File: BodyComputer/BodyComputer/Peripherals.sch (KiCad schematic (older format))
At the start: 17 parts

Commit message: Update due to moving to another computer. Updated Schematic, Print-outs, PCB in development
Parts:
- added J13, J9: Conn_02x05_Odd_Even, Connector_IDC:IDC-Header_2x05_P2.54mm_Vertical, symbol Connector_Generic:Conn_02x05_Odd_Even
- added J35: Conn_01x02, Connector_PinSocket_2.54mm:PinSocket_1x02_P2.54mm_Vertical, symbol Connector_Generic:Conn_01x02
- D11: renamed from D?; footprint (none) -> Diode_SMD:D_0603_1608Metric_Pad1.05x0.95mm_HandSolder
- SW1: renamed from SW?; footprint (none) -> Button_Switch_THT:SW_PUSH_6mm
- gave numbers to parts that had none: 15
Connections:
- net +3V3: now also J14.3 (Pin_3), J14.5 (Pin_5), J14.7 (Pin_7)
- net GND: now also J14.1 (Pin_1), J14.10 (Pin_10), J14.9 (Pin_9), J13.6 (Pin_6), J35.2 (Pin_2), J9.6 (Pin_6)
- net MISO: now also J11.2; no longer J11.3
- net MOSI: now also J11.3; no longer J11.4
- net RESET_BUTTON: now also J9.8 (Pin_8)
- net RX: now also J11.5; no longer J11.1
- net SCK: now also J11.1; no longer J11.5
- net TX: now also J11.4; no longer J11.2
- net at U5.1 (A0(ADC0)): now also J9.9 (Pin_9)
- net at U5.11 (3.3V): now also J9.10 (Pin_10)
- net at U5.18 (TX(GPIO1)): now also J13.2 (Pin_2)
- net at U5.19 (RX(DPIO3)): now also J13.4 (Pin_4)
- net at U5.22 (D6(GPIO12)): now also J13.8 (Pin_8)
- net at U5.23 (D5(GPIO14)): now also J13.10 (Pin_10)
- net at U5.25 (3.3V): now also J13.9 (Pin_9)
- net at U5.26 (D4(GPIO2)): now also J13.7 (Pin_7)
- net at U5.27 (D3(GPIO0)): now also J13.5 (Pin_5)
- net at U5.28 (D2(GPIO4)): now also J13.3 (Pin_3)
- net at U5.29 (D1(GPIO5)): now also J13.1 (Pin_1)
- net at U5.4 (SD3(GPIO10)): now also J9.7 (Pin_7)
- net at U5.5 (SD2(GPIO9)): now also J9.5 (Pin_5)
- net at U5.6 (SD1(MOSI)): now also J9.3 (Pin_3)
- net at U5.7 (CMD(CS)): now also J9.1 (Pin_1)
- net at U5.8 (SDO(MISO)): now also J9.2 (Pin_2)
- net at U5.9 (CLK(SCLK)): now also J9.4 (Pin_4)
- new net VIN: J35.1 (Pin_1)
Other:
- note added: "FAN connector"
- note added: "NodeMCU v3 and external connectors (IDC10)"
- moved on the sheet: D11, J14, R27, U5

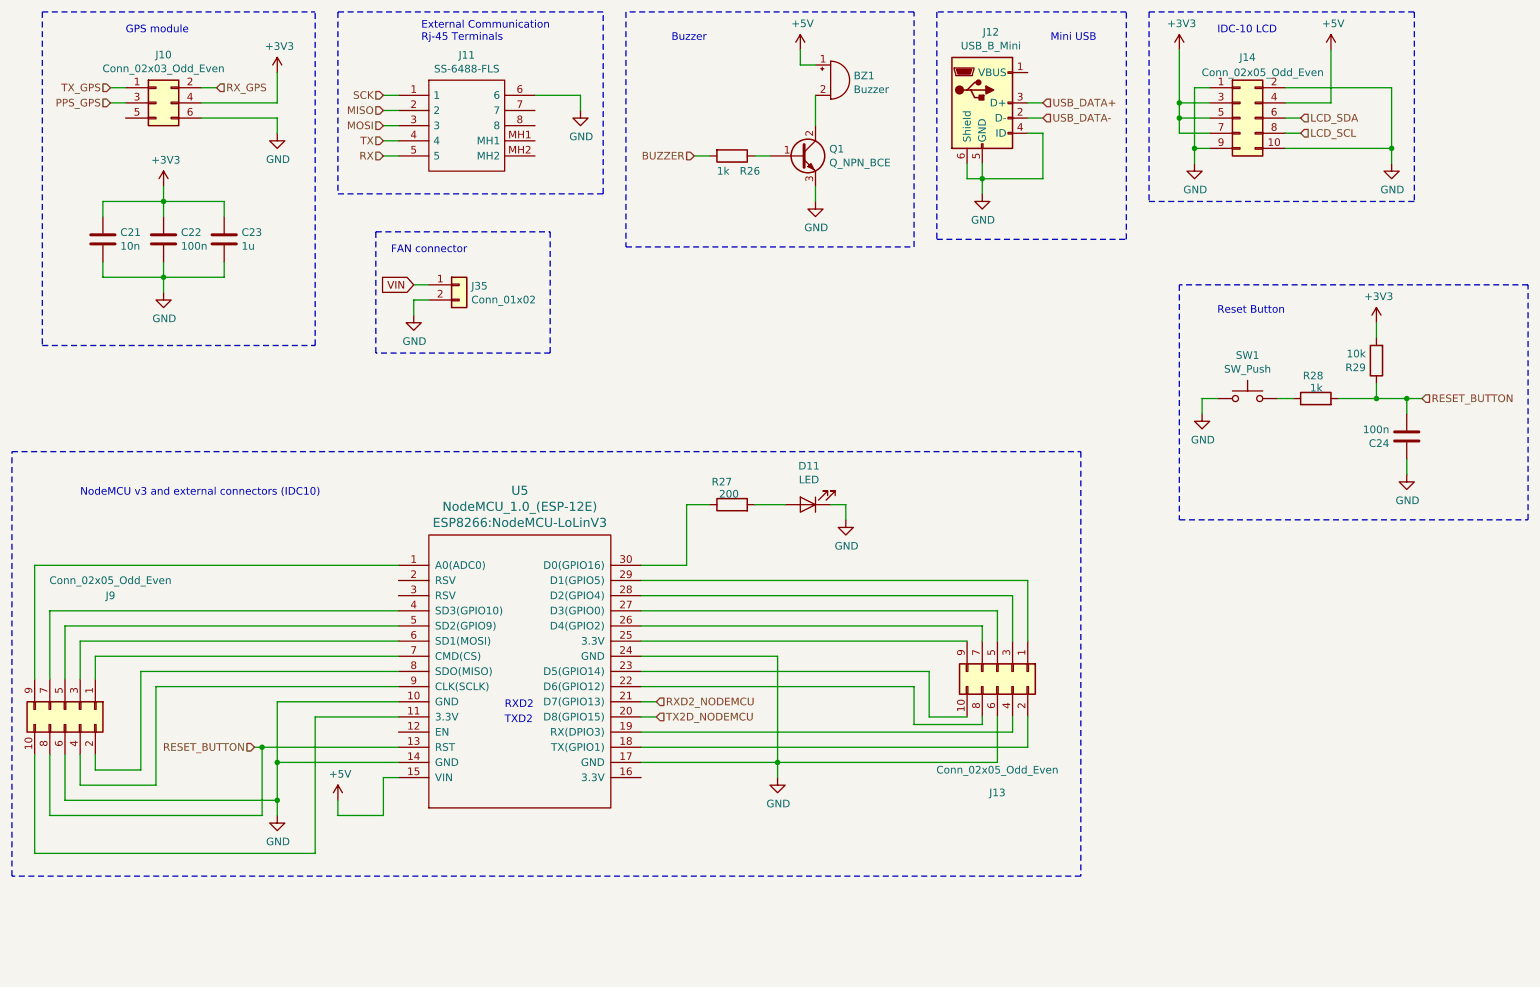
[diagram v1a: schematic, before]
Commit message: Updated schematic (DC/DC), 2-layer PCB
Updated schematic in multiple places, added elements, exchanged 3V3 stabilizer for a DC/DC converter. Nearly finished 2-layer PCB layout.
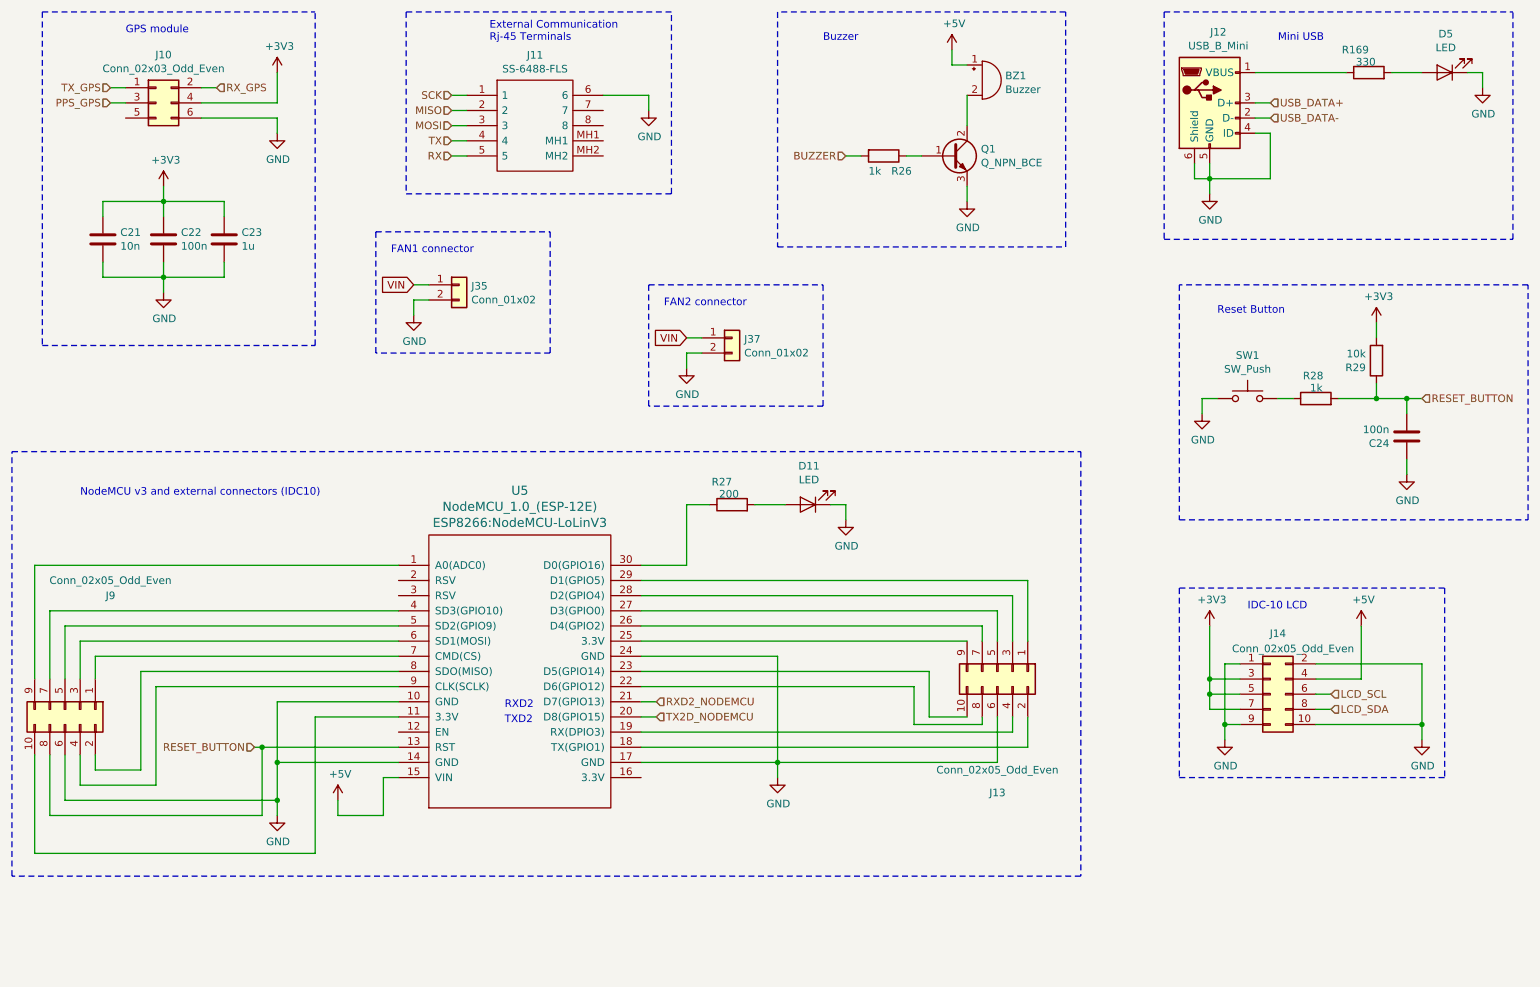
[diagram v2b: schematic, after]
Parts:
- added D5: LED, Diode_SMD:D_0603_1608Metric_Pad1.05x0.95mm_HandSolder, symbol Device:LED
- added J37: Conn_01x02, Connector_PinSocket_2.54mm:PinSocket_1x02_P2.54mm_Vertical, symbol Connector_Generic:Conn_01x02
- added R169: 330, Resistor_SMD:R_0603_1608Metric, symbol Device:R
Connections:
- net GND: now also D5.1 (K), J37.2 (Pin_2)
- net LCD_SCL: now also J14.6 (Pin_6); no longer J14.8 (Pin_8)
- net LCD_SDA: now also J14.8 (Pin_8); no longer J14.6 (Pin_6)
- net VIN: now also J37.1 (Pin_1)
- net at J12.1 (VBUS): now also R169.1
- new net: D5.2 (A), R169.2
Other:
- note added: "FAN1 connector"
- note added: "FAN2 connector"
- note removed: "FAN connector"
- moved on the sheet: BZ1, J11, J12, J14, Q1, R26

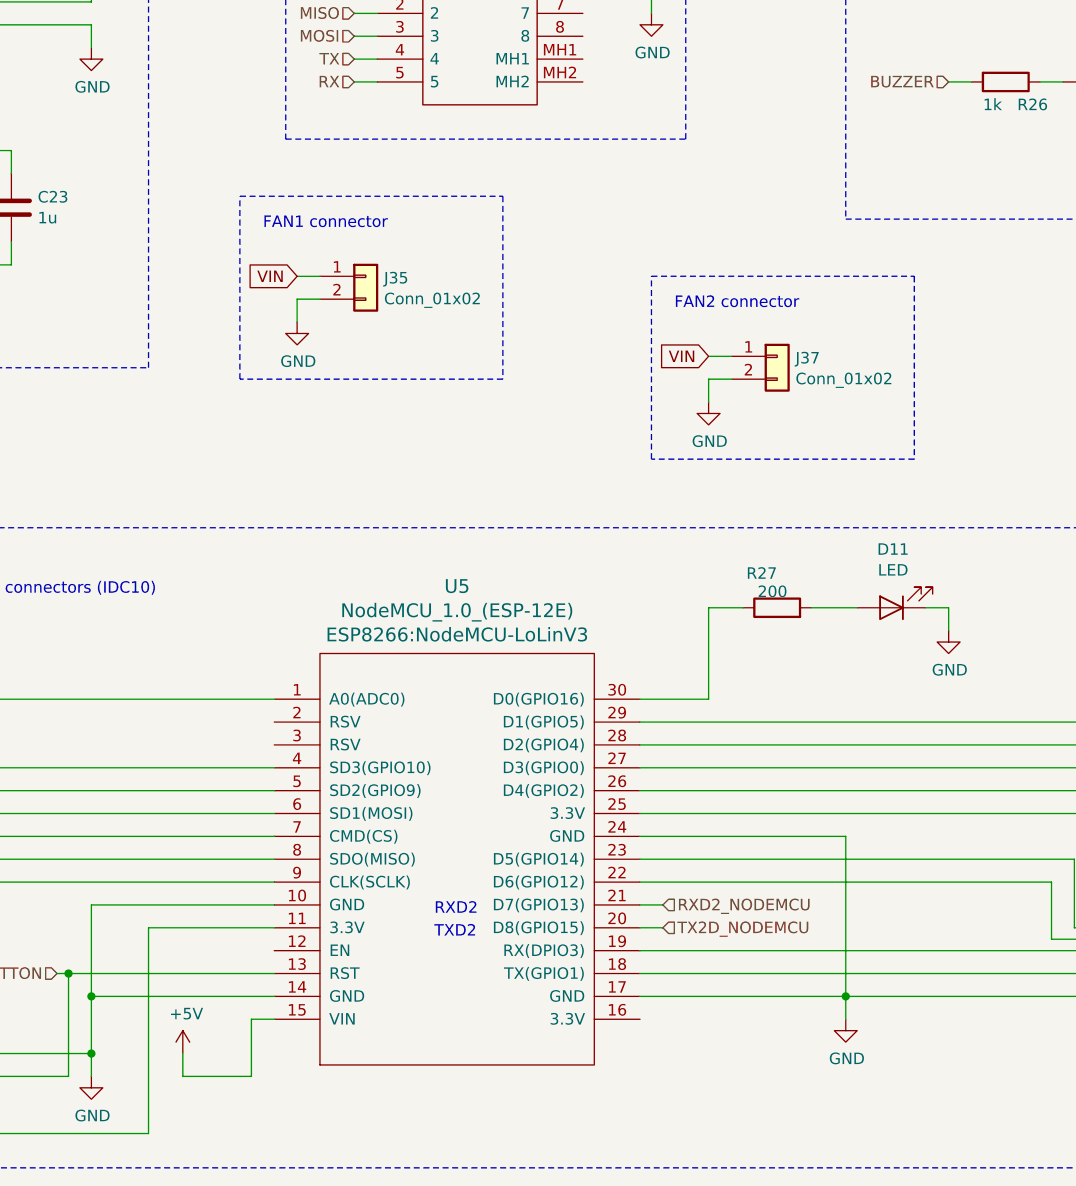
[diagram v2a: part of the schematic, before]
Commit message: Body Computer - 4layer
Added 4-layer board layout, changed schematic a bit, added jumper for NodeMCU powering, control MOSFET for Fans
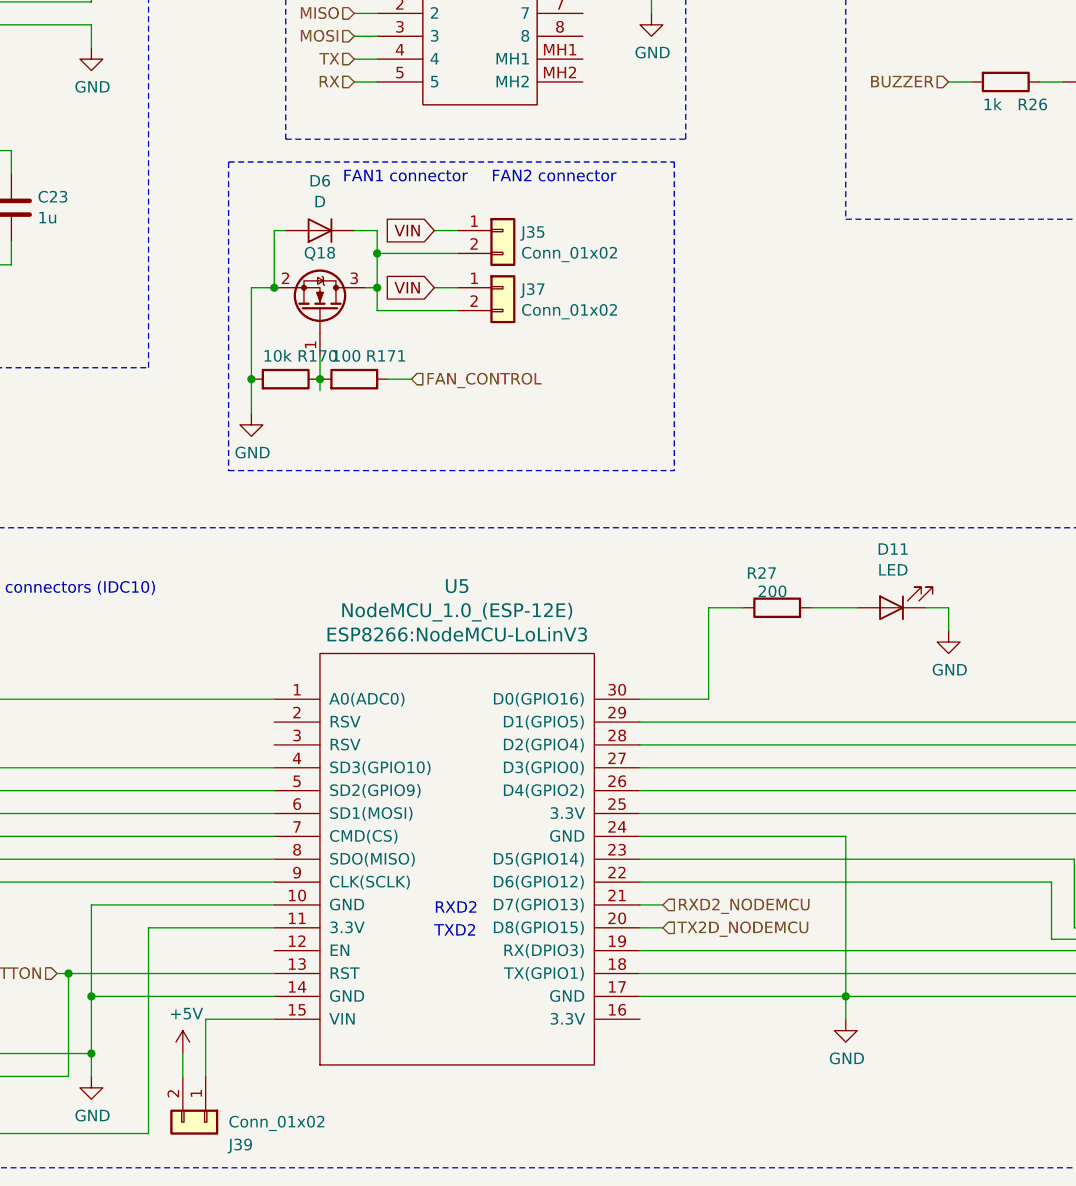
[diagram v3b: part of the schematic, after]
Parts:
- added D6: D, Diode_SMD:D_SMA, symbol Device:D
- added J39: Conn_01x02, Connector_PinSocket_2.54mm:PinSocket_1x02_P2.54mm_Vertical, symbol Connector_Generic:Conn_01x02
- added Q18: IRLML2060, Package_TO_SOT_SMD:SOT-23, symbol Transistor_FET:IRLML2060
- added R170: 10k, Resistor_SMD:R_0603_1608Metric, symbol Device:R
- added R171: 100, Resistor_SMD:R_0603_1608Metric, symbol Device:R
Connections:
- net +5V: now also J39.2 (Pin_2); no longer U5.15 (VIN)
- net GND: now also D6.2 (A), Q18.2 (S), R170.2; no longer J35.2 (Pin_2), J37.2 (Pin_2)
- new net: J39.1 (Pin_1), U5.15 (VIN)
- new net: D6.1 (K), J35.2 (Pin_2), J37.2 (Pin_2), Q18.3 (D)
- new net: Q18.1 (G), R170.1, R171.2
- new net FAN_CONTROL: R171.1
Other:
- moved on the sheet: J35, J37
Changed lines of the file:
@@
 Sheet 4 7
 Title "Body Computer"
-Date "2020-04-01"
+Date "2020-04-12"
 Rev "1.0"
 Comp "Wojciech Grzeliński"
@@
 $EndComp
 Wire Wire Line
-	3350 5750 3250 5750
-Wire Wire Line
-	3250 5750 3250 6000
-Wire Wire Line
-	3250 6000 2950 6000
-Wire Wire Line
 	2950 6000 2950 5900
 Wire Wire Line
@@
 L Connector_Generic:Conn_01x02 J35
 U 1 1 5FE3C840
-P 3750 2500
-F 0 "J35" H 3830 2492 50  0000 L CNN
-F 1 "Conn_01x02" H 3830 2401 50  0000 L CNN
-F 2 "Connector_PinSocket_2.54mm:PinSocket_1x02_P2.54mm_Vertical" H 3750 2500 50  0001 C CNN
-F 3 "~" H 3750 2500 50  0001 C CNN
-	1    3750 2500
-	1    0    0    -1
-$EndComp
-Wire Wire Line
-	3550 2500 3450 2500
-Wire Wire Line
-	3550 2600 3450 2600
-Wire Wire Line
-	3450 2600 3450 2700
-$Comp
-L power:GND #PWR?
-U 1 1 5FE49DD6
-P 3450 2700
-AR Path="/5F25F1A8/5FE49DD6" Ref="#PWR?"  Part="1"
-AR Path="/5E6DC799/5FE49DD6" Ref="#PWR0141"  Part="1"
-F 0 "#PWR0141" H 3450 2450 50  0001 C CNN
-F 1 "GND" H 3455 2527 50  0000 C CNN
-F 2 "" H 3450 2700 50  0001 C CNN
-F 3 "" H 3450 2700 50  0001 C CNN
-	1    3450 2700
-	1    0    0    -1
-$EndComp
-Text GLabel 3450 2500 0    50   Input ~ 0
+P 4350 2300
+F 0 "J35" H 4430 2292 50  0000 L CNN
+F 1 "Conn_01x02" H 4430 2201 50  0000 L CNN
+F 2 "Connector_PinSocket_2.54mm:PinSocket_1x02_P2.54mm_Vertical" H 4350 2300 50  0001 C CNN
+F 3 "~" H 4350 2300 50  0001 C CNN
+	1    4350 2300
+	1    0    0    -1
+$EndComp
+Wire Wire Line
+	4150 2300 4050 2300
+Text GLabel 4050 2300 0    50   Input ~ 0
 VIN
-Text Notes 3300 2300 0    50   ~ 0
+Text Notes 3650 2100 0    50   ~ 0
 FAN1 connector
-Wire Notes Line
-	4350 2150 4350 2950
-Wire Notes Line
-	4350 2950 3200 2950
-Wire Notes Line
-	3200 2950 3200 2150
-Wire Notes Line
-	3200 2150 4350 2150
 $Comp
 L Connector_Generic:Conn_01x02 J37
 U 1 1 5E8F875D
-P 5550 2850
-F 0 "J37" H 5630 2842 50  0000 L CNN
-F 1 "Conn_01x02" H 5630 2751 50  0000 L CNN
-F 2 "Connector_PinSocket_2.54mm:PinSocket_1x02_P2.54mm_Vertical" H 5550 2850 50  0001 C CNN
-F 3 "~" H 5550 2850 50  0001 C CNN
-	1    5550 2850
-	1    0    0    -1
-$EndComp
-Wire Wire Line
-	5350 2850 5250 2850
-Wire Wire Line
-	5350 2950 5250 2950
-Wire Wire Line
-	5250 2950 5250 3050
-$Comp
-L power:GND #PWR?
-U 1 1 5E8F8766
-P 5250 3050
-AR Path="/5F25F1A8/5E8F8766" Ref="#PWR?"  Part="1"
-AR Path="/5E6DC799/5E8F8766" Ref="#PWR0147"  Part="1"
-F 0 "#PWR0147" H 5250 2800 50  0001 C CNN
-F 1 "GND" H 5255 2877 50  0000 C CNN
-F 2 "" H 5250 3050 50  0001 C CNN
-F 3 "" H 5250 3050 50  0001 C CNN
-	1    5250 3050
-	1    0    0    -1
-$EndComp
-Text GLabel 5250 2850 0    50   Input ~ 0
+P 4350 2550
+F 0 "J37" H 4430 2542 50  0000 L CNN
+F 1 "Conn_01x02" H 4430 2451 50  0000 L CNN
+F 2 "Connector_PinSocket_2.54mm:PinSocket_1x02_P2.54mm_Vertical" H 4350 2550 50  0001 C CNN
+F 3 "~" H 4350 2550 50  0001 C CNN
+	1    4350 2550
+	1    0    0    -1
+$EndComp
+Wire Wire Line
+	4150 2550 4050 2550
+Text GLabel 4050 2550 0    50   Input ~ 0
 VIN
-Text Notes 5100 2650 0    50   ~ 0
+Text Notes 4300 2100 0    50   ~ 0
 FAN2 connector
-Wire Notes Line
-	6150 2500 6150 3300
-Wire Notes Line
-	6150 3300 5000 3300
-Wire Notes Line
-	5000 3300 5000 2500
-Wire Notes Line
-	5000 2500 6150 2500
 $Comp
 L Device:R R?
@@
 Wire Notes Line
 	8400 700  10700 700
+$Comp
+L Device:R R?
+U 1 1 5E9991C0
+P 3700 2950
+AR Path="/5E667041/5E9991C0" Ref="R?"  Part="1"
+AR Path="/5E731526/5E9991C0" Ref="R?"  Part="1"
+AR Path="/5E6DC799/5E9991C0" Ref="R171"  Part="1"
+F 0 "R171" V 3800 3000 50  0000 L CNN
+F 1 "100" V 3800 2850 50  0000 L CNN
+F 2 "Resistor_SMD:R_0603_1608Metric" V 3630 2950 50  0001 C CNN
+F 3 "~" H 3700 2950 50  0001 C CNN
+	1    3700 2950
+	0    1    -1   0
+$EndComp
+Wire Wire Line
+	3800 2550 3750 2550
+$Comp
+L Device:D D?
+U 1 1 5E9991CE
+P 3550 2300
+AR Path="/5E731526/5E9991CE" Ref="D?"  Part="1"
+AR Path="/5E6DC799/5E9991CE" Ref="D6"  Part="1"
+F 0 "D6" H 3550 2084 50  0000 C CNN
+F 1 "D" H 3550 2175 50  0000 C CNN
+F 2 "Diode_SMD:D_SMA" H 3550 2300 50  0001 C CNN
+F 3 "~" H 3550 2300 50  0001 C CNN
+	1    3550 2300
+	-1   0    0    1
+$EndComp
+Wire Wire Line
+	3800 2300 3800 2400
+Wire Wire Line
+	3700 2300 3800 2300
+Wire Wire Line
+	3400 2300 3350 2300
+Wire Wire Line
+	3350 2300 3350 2550
+$Comp
+L power:GND #PWR?
+U 1 1 5E9991E5
+P 3250 3100
+AR Path="/5F25F1A8/5E9991E5" Ref="#PWR?"  Part="1"
+AR Path="/5E6DC799/5E9991E5" Ref="#PWR0141"  Part="1"
+AR Path="/5E667041/5E9991E5" Ref="#PWR?"  Part="1"
+AR Path="/5E6671BF/5E9991E5" Ref="#PWR?"  Part="1"
+AR Path="/5E731526/5E9991E5" Ref="#PWR?"  Part="1"
+F 0 "#PWR0141" H 3250 2850 50  0001 C CNN
+F 1 "GND" H 3255 2927 50  0000 C CNN
+F 2 "" H 3250 3100 50  0001 C CNN
+F 3 "" H 3250 3100 50  0001 C CNN
+	1    3250 3100
+	1    0    0    -1
+$EndComp
+Wire Wire Line
+	3250 2550 3350 2550
+$Comp
+L Device:R R?
+U 1 1 5E9991ED
+P 3400 2950
+AR Path="/5E667041/5E9991ED" Ref="R?"  Part="1"
+AR Path="/5E731526/5E9991ED" Ref="R?"  Part="1"
+AR Path="/5E6DC799/5E9991ED" Ref="R170"  Part="1"
+F 0 "R170" V 3500 3000 50  0000 L CNN
+F 1 "10k" V 3500 2850 50  0000 L CNN
+F 2 "Resistor_SMD:R_0603_1608Metric" V 3330 2950 50  0001 C CNN
+F 3 "~" H 3400 2950 50  0001 C CNN
+	1    3400 2950
+	0    1    -1   0
+$EndComp
+Wire Wire Line
+	3550 3000 3550 2950
+Wire Wire Line
+	3550 2850 3550 2950
+Connection ~ 3550 2950
+Wire Wire Line
+	3800 2400 4150 2400
+Connection ~ 3800 2400
+Wire Wire Line
+	3800 2400 3800 2550
+Connection ~ 3350 2550
+$Comp
+L Transistor_FET:IRLML2060 Q?
+U 1 1 5E9991BA
+P 3550 2650
+AR Path="/5E664F82/5E9991BA" Ref="Q?"  Part="1"
+AR Path="/5E731526/5E9991BA" Ref="Q?"  Part="1"
+AR Path="/5E6DC799/5E9991BA" Ref="Q18"  Part="1"
+F 0 "Q18" V 3801 2650 50  0000 C CNN
+F 1 "IRLML2060" H 3754 2605 50  0001 L CNN
+F 2 "Package_TO_SOT_SMD:SOT-23" H 3750 2575 50  0001 L CIN
+F 3 "https://www.infineon.com/dgdl/irlml2060pbf.pdf?fileId=5546d462533600a401535664b7fb25ee" H 3550 2650 50  0001 L CNN
+	1    3550 2650
+	0    1    -1   0
+$EndComp
+Wire Wire Line
+	3250 2550 3250 2950
+Wire Wire Line
+	3250 3100 3250 2950
+Connection ~ 3250 2950
+Wire Wire Line
+	3850 2950 3950 2950
+Wire Wire Line
+	3800 2650 3800 2550
+Wire Wire Line
+	3800 2650 4150 2650
+Connection ~ 3800 2550
+Wire Notes Line
+	3150 2000 5100 2000
+Wire Notes Line
+	3150 2000 3150 3350
+Wire Notes Line
+	5100 2000 5100 3350
+Wire Notes Line
+	3150 3350 5100 3350
+Text HLabel 3950 2950 2    50   Input ~ 0
+FAN_CONTROL
+$Comp
+L Connector_Generic:Conn_01x02 J39
+U 1 1 5EAB39B7
+P 3050 6200
+F 0 "J39" V 3150 6300 50  0000 L CNN
+F 1 "Conn_01x02" V 3050 6300 50  0000 L CNN
+F 2 "Connector_PinSocket_2.54mm:PinSocket_1x02_P2.54mm_Vertical" H 3050 6200 50  0001 C CNN
+F 3 "~" H 3050 6200 50  0001 C CNN
+	1    3050 6200
+	0    1    1    0
+$EndComp
+Wire Wire Line
+	3050 6000 3050 5750
+Wire Wire Line
+	3050 5750 3350 5750
 $EndSCHEMATC
